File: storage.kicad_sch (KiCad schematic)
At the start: 1 part, among them U1 MIMX8MN5DVPIZAA

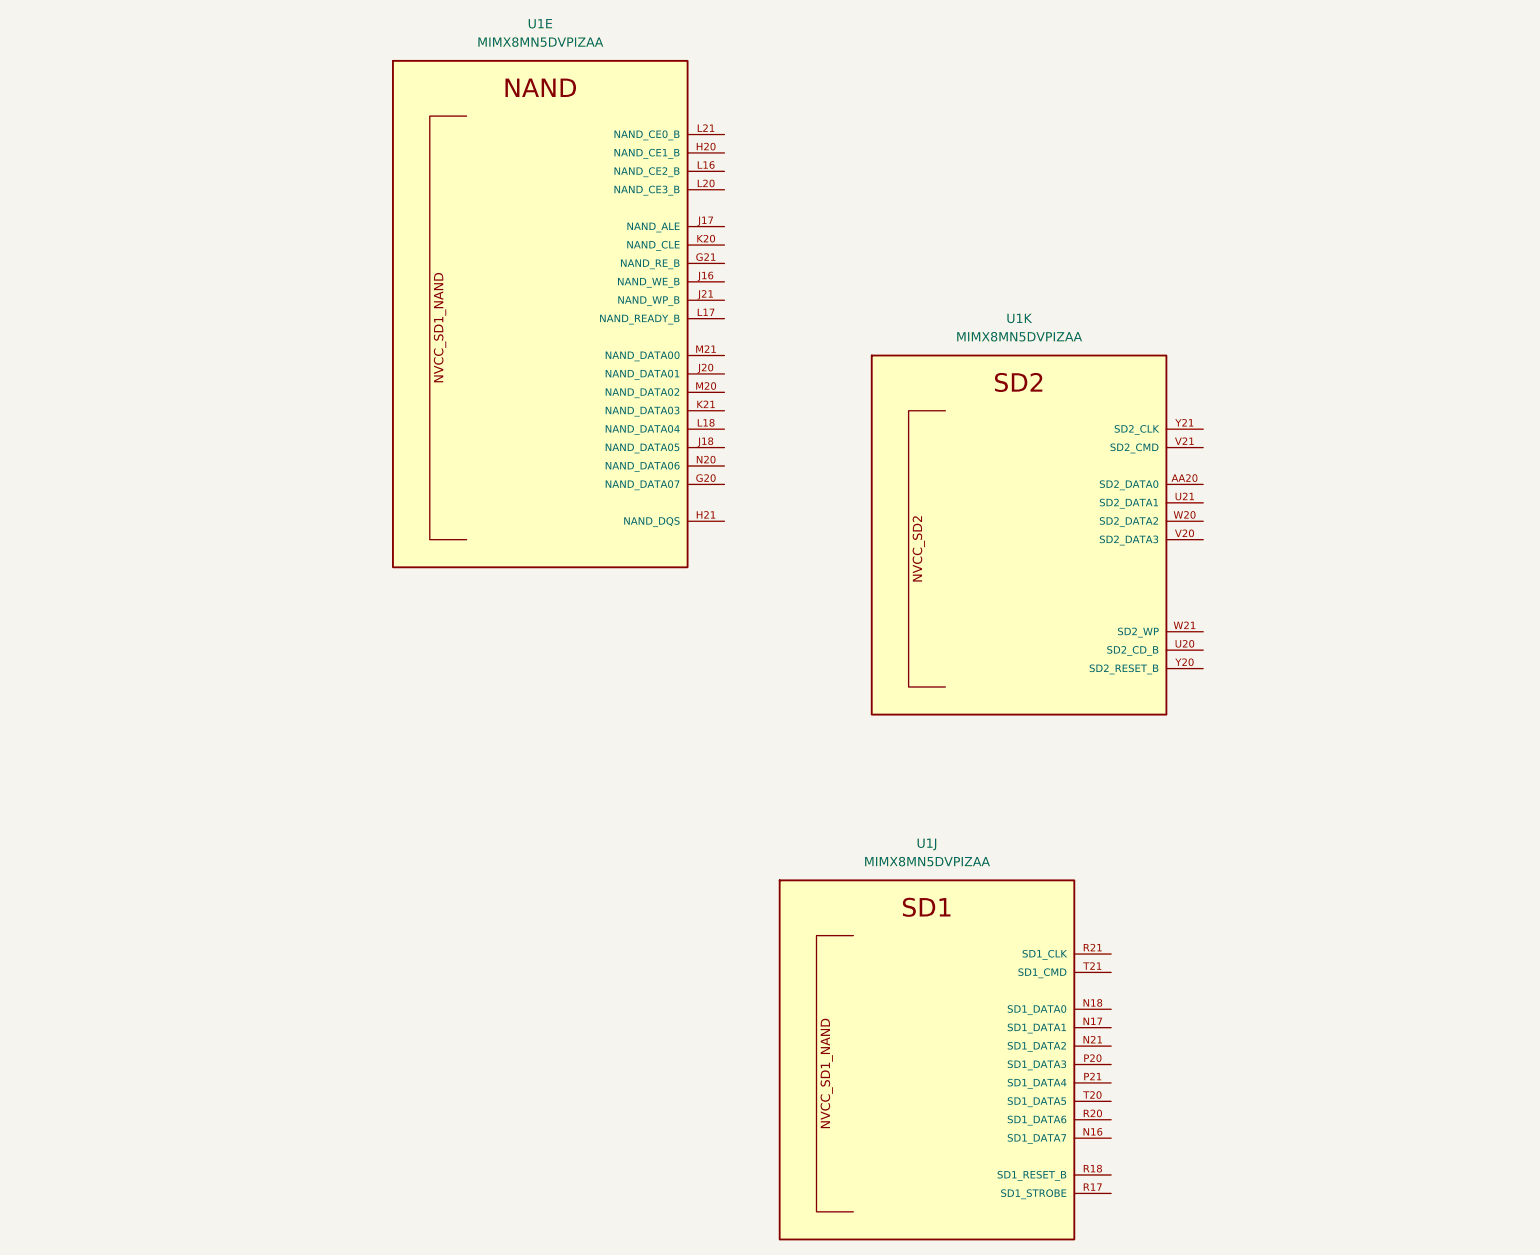
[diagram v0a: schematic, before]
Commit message: move to i.MX8M Mini
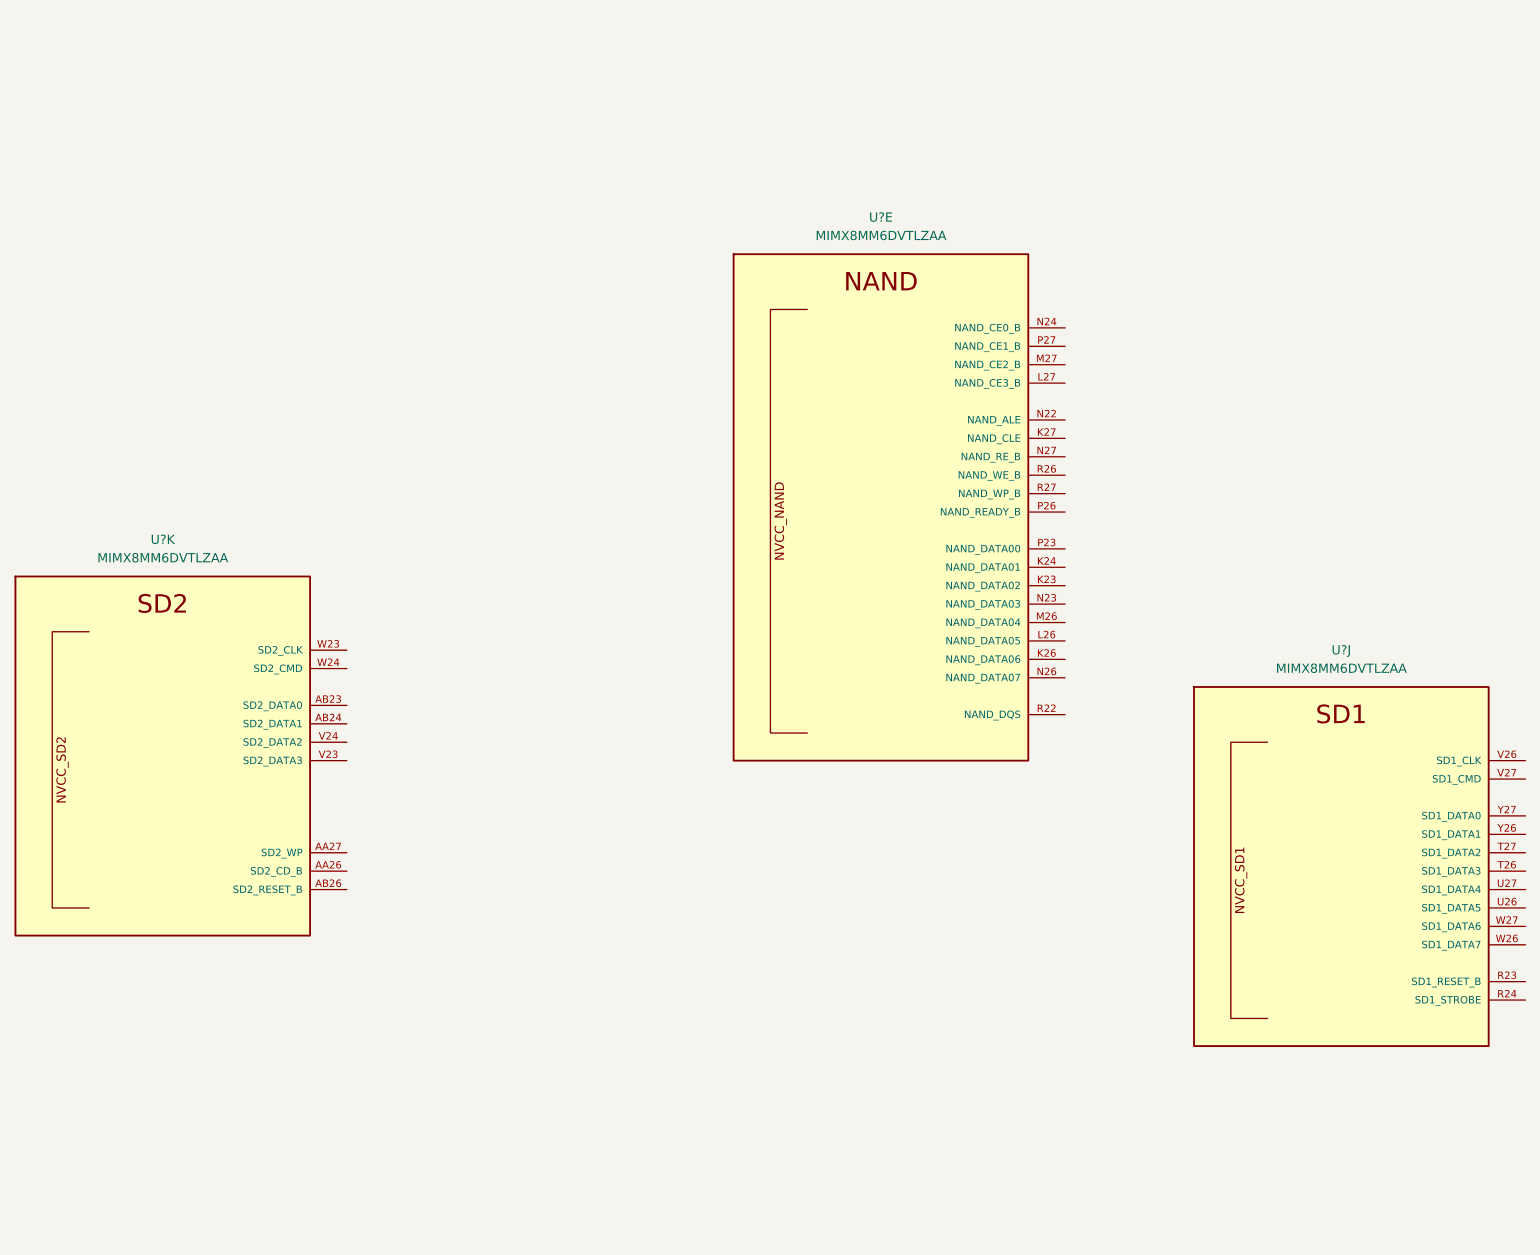
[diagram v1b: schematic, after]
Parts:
- removed U1: MIMX8MN5DVPIZAA, qsbc:SOT1967-1, symbol qsbc:MIMX8MN5DVPIZAA
- added U? (x3): MIMX8MM6DVTLZAA, qsbc:SOT1967-1, symbol qsbc:MIMX8MM6DVTLZAA

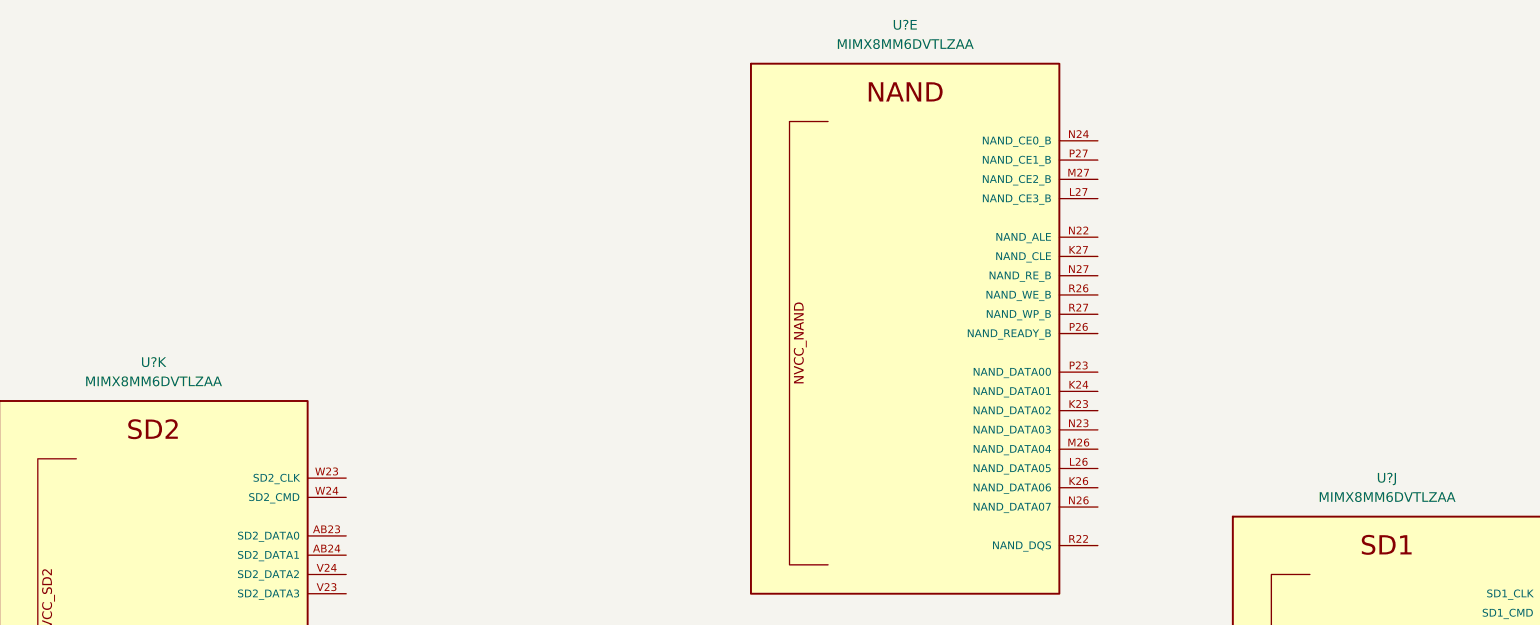
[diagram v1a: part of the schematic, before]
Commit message: ddr sch done
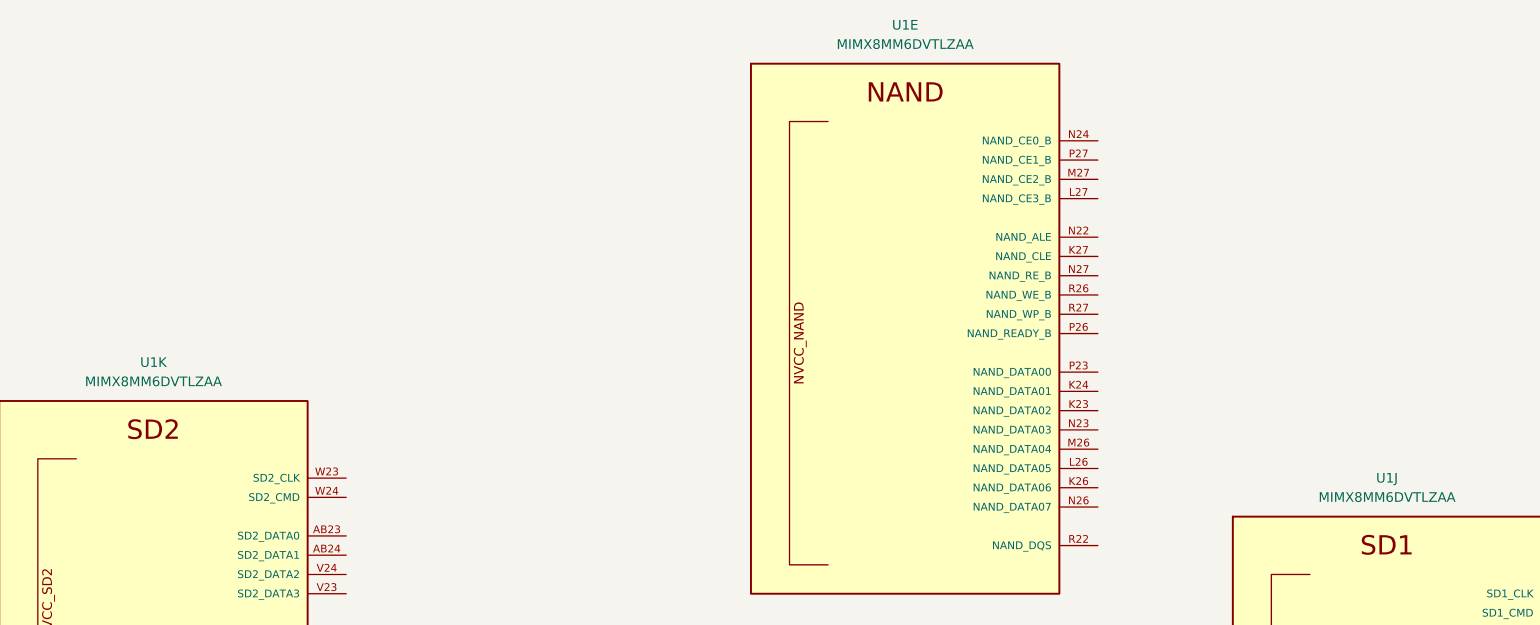
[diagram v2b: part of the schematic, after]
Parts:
- gave numbers to parts that had none: 1
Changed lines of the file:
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@@
   (symbol (lib_id "qsbc:MIMX8MM6DVTLZAA") (at 210.82 121.92 0) (unit 10)
     (in_bom yes) (on_board yes) (fields_autoplaced)
-    (property "Reference" "U?" (id 0) (at 210.82 102.87 0))
+    (property "Reference" "U1" (id 0) (at 210.82 102.87 0))
     (property "Value" "MIMX8MM6DVTLZAA" (id 1) (at 210.82 105.41 0))
     (property "Footprint" "qsbc:SOT1967-1" (id 2) (at 214.63 312.42 0)
@@
   (symbol (lib_id "qsbc:MIMX8MM6DVTLZAA") (at 147.32 62.23 0) (unit 5)
     (in_bom yes) (on_board yes) (fields_autoplaced)
-    (property "Reference" "U?" (id 0) (at 147.32 43.18 0))
+    (property "Reference" "U1" (id 0) (at 147.32 43.18 0))
     (property "Value" "MIMX8MM6DVTLZAA" (id 1) (at 147.32 45.72 0))
     (property "Footprint" "qsbc:SOT1967-1" (id 2) (at 151.13 252.73 0)
@@
   (symbol (lib_id "qsbc:MIMX8MM6DVTLZAA") (at 48.26 106.68 0) (unit 11)
     (in_bom yes) (on_board yes) (fields_autoplaced)
-    (property "Reference" "U?" (id 0) (at 48.26 87.63 0))
+    (property "Reference" "U1" (id 0) (at 48.26 87.63 0))
     (property "Value" "MIMX8MM6DVTLZAA" (id 1) (at 48.26 90.17 0))
     (property "Footprint" "qsbc:SOT1967-1" (id 2) (at 52.07 297.18 0)

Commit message: misc work, usb sch done
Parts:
- added J5: Micro_SD_Card_Det1, symbol qsbc:Micro_SD_Card_Det1
- added U15: W25Q32JVZP, Package_SON:WSON-8-1EP_6x5mm_P1.27mm_EP3.4x4.3mm, symbol Memory_Flash:W25Q32JVZP
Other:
- moved on the sheet: U1E, U1J, U1K
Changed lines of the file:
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@@
 (kicad_sch (version 20211123) (generator eeschema)
-  (paper "A4")
-  (symbol (lib_id "qsbc:MIMX8MM6DVTLZAA") (at 210.82 121.92 0) (unit 10)
+  (paper "A3")
+  (symbol (lib_id "qsbc:Micro_SD_Card_Det1") (at 156.21 208.28 0) (unit 1)
     (in_bom yes) (on_board yes) (fields_autoplaced)
-    (property "Reference" "U1" (id 0) (at 210.82 102.87 0))
-    (property "Value" "MIMX8MM6DVTLZAA" (id 1) (at 210.82 105.41 0))
-    (property "Footprint" "qsbc:SOT1967-1" (id 2) (at 214.63 312.42 0)
+    (property "Reference" "J5" (id 0) (at 156.845 189.23 0))
+    (property "Value" "Micro_SD_Card_Det1" (id 1) (at 156.845 191.77 0))
+    (property "Footprint" "" (id 2) (at 185.42 200.66 0)
+      (effects (font (size 1.27 1.27)) hide)
+    )
+    (property "Datasheet" "" (id 3) (at 156.21 208.28 0)
+      (effects (font (size 1.27 1.27)) hide)
+    )
+    (pin "1")
+    (pin "10")
+    (pin "2")
+    (pin "3")
+    (pin "4")
+    (pin "5")
+    (pin "6")
+    (pin "7")
+    (pin "8")
+    (pin "9")
+  )
+  (symbol (lib_id "qsbc:MIMX8MM6DVTLZAA") (at 360.68 203.2 0) (unit 10)
+    (in_bom yes) (on_board yes) (fields_autoplaced)
+    (property "Reference" "U1" (id 0) (at 360.68 184.15 0))
+    (property "Value" "MIMX8MM6DVTLZAA" (id 1) (at 360.68 186.69 0))
+    (property "Footprint" "qsbc:SOT1967-1" (id 2) (at 364.49 393.7 0)
       (effects (font (size 1.27 1.27)) (justify left bottom) hide)
     )
-    (property "Datasheet" "https://www.nxp.com/docs/en/data-sheet/IMX8MMCEC.pdf" (id 3) (at 212.09 316.23 0)
+    (property "Datasheet" "https://www.nxp.com/docs/en/data-sheet/IMX8MMCEC.pdf" (id 3) (at 361.95 397.51 0)
       (effects (font (size 1.27 1.27)) (justify left bottom) hide)
     )
@@
     (pin "D19")
   )
-  (symbol (lib_id "qsbc:MIMX8MM6DVTLZAA") (at 147.32 62.23 0) (unit 5)
+  (symbol (lib_id "Memory_Flash:W25Q32JVZP") (at 144.78 74.93 0) (unit 1)
     (in_bom yes) (on_board yes) (fields_autoplaced)
-    (property "Reference" "U1" (id 0) (at 147.32 43.18 0))
-    (property "Value" "MIMX8MM6DVTLZAA" (id 1) (at 147.32 45.72 0))
-    (property "Footprint" "qsbc:SOT1967-1" (id 2) (at 151.13 252.73 0)
+    (property "Reference" "U15" (id 0) (at 146.7994 62.23 0)
+      (effects (font (size 1.27 1.27)) (justify left))
+    )
+    (property "Value" "W25Q32JVZP" (id 1) (at 146.7994 64.77 0)
+      (effects (font (size 1.27 1.27)) (justify left))
+    )
+    (property "Footprint" "Package_SON:WSON-8-1EP_6x5mm_P1.27mm_EP3.4x4.3mm" (id 2) (at 144.78 74.93 0)
+      (effects (font (size 1.27 1.27)) hide)
+    )
+    (property "Datasheet" "http://www.winbond.com/resource-files/w25q32jv%20revg%2003272018%20plus.pdf" (id 3) (at 144.78 74.93 0)
+      (effects (font (size 1.27 1.27)) hide)
+    )
+    (pin "1")
+    (pin "2")
+    (pin "3")
+    (pin "4")
+    (pin "5")
+    (pin "6")
+    (pin "7")
+    (pin "8")
+    (pin "9")
+  )
+  (symbol (lib_id "qsbc:MIMX8MM6DVTLZAA") (at 81.28 60.96 0) (unit 5)
+    (in_bom yes) (on_board yes) (fields_autoplaced)
+    (property "Reference" "U1" (id 0) (at 81.28 41.91 0))
+    (property "Value" "MIMX8MM6DVTLZAA" (id 1) (at 81.28 44.45 0))
+    (property "Footprint" "qsbc:SOT1967-1" (id 2) (at 85.09 251.46 0)
       (effects (font (size 1.27 1.27)) (justify left bottom) hide)
     )
-    (property "Datasheet" "https://www.nxp.com/docs/en/data-sheet/IMX8MMCEC.pdf" (id 3) (at 148.59 256.54 0)
+    (property "Datasheet" "https://www.nxp.com/docs/en/data-sheet/IMX8MMCEC.pdf" (id 3) (at 82.55 255.27 0)
       (effects (font (size 1.27 1.27)) (justify left bottom) hide)
     )
@@
     (pin "D19")
   )
-  (symbol (lib_id "qsbc:MIMX8MM6DVTLZAA") (at 48.26 106.68 0) (unit 11)
+  (symbol (lib_id "qsbc:MIMX8MM6DVTLZAA") (at 59.69 210.82 0) (unit 11)
     (in_bom yes) (on_board yes) (fields_autoplaced)
-    (property "Reference" "U1" (id 0) (at 48.26 87.63 0))
-    (property "Value" "MIMX8MM6DVTLZAA" (id 1) (at 48.26 90.17 0))
-    (property "Footprint" "qsbc:SOT1967-1" (id 2) (at 52.07 297.18 0)
+    (property "Reference" "U1" (id 0) (at 59.69 191.77 0))
+    (property "Value" "MIMX8MM6DVTLZAA" (id 1) (at 59.69 194.31 0))
+    (property "Footprint" "qsbc:SOT1967-1" (id 2) (at 63.5 401.32 0)
       (effects (font (size 1.27 1.27)) (justify left bottom) hide)
     )
-    (property "Datasheet" "https://www.nxp.com/docs/en/data-sheet/IMX8MMCEC.pdf" (id 3) (at 49.53 300.99 0)
+    (property "Datasheet" "https://www.nxp.com/docs/en/data-sheet/IMX8MMCEC.pdf" (id 3) (at 60.96 405.13 0)
       (effects (font (size 1.27 1.27)) (justify left bottom) hide)
     )
